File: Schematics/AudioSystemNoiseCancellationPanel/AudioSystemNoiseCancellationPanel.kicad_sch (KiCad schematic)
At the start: 7 parts, among them J1 AudioJack2, U1 OPA134

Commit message: progress check
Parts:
- removed J1: AudioJack2, symbol Connector_Audio:AudioJack2
- added C3: 1u, symbol Device:C_Small
- added C4: 0.1u, symbol Device:C_Small
- added U2: MIC5365-1.2YC5-TR, MIC5365-1.2YC5-TR:SOT65P210X110-5N, symbol AudioSystemSymbolLibrary:MIC5365-1.2YC5-TR
- C1: value 0.1u -> 1u
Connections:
- net GND: now also C3.2, C4.2, U2.2 (GND)
- net ANCSignal: now reaches R2.2, U1.6
- net -5VMic: now reaches U1.4 (V-)
- net +5VMic: now reaches U1.7 (V+)
- net +5VMic: now also C3.1, U2.1 (VIN), U2.3 (EN)
- net +1V1: no longer names the net of C1.1, MK1.3 (VDD)
- net +1V1: now also C4.1, U2.5 (VOUT)
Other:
- moved on the sheet: C2, MK1, R1, R2, U1

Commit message: power supply schematic possibly done
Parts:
- U2: footprint MIC5365-1.2YC5-TR:SOT65P210X110-5N -> AudioSystemFootprintLibrary:MIC5365-1.2YC5-TR
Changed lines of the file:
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@@
 		(on_board yes)
 		(dnp no)
-		(fields_autoplaced yes)
 		(property "Reference" "MK1"
 			(at 132.08 109.22 0)
@@
 			)
 		)
-		(property "Footprint" "MIC5365-1.2YC5-TR:SOT65P210X110-5N"
+		(property "Footprint" "AudioSystemFootprintLibrary:MIC5365-1.2YC5-TR"
 			(at 109.22 88.9 0)
 			(effects

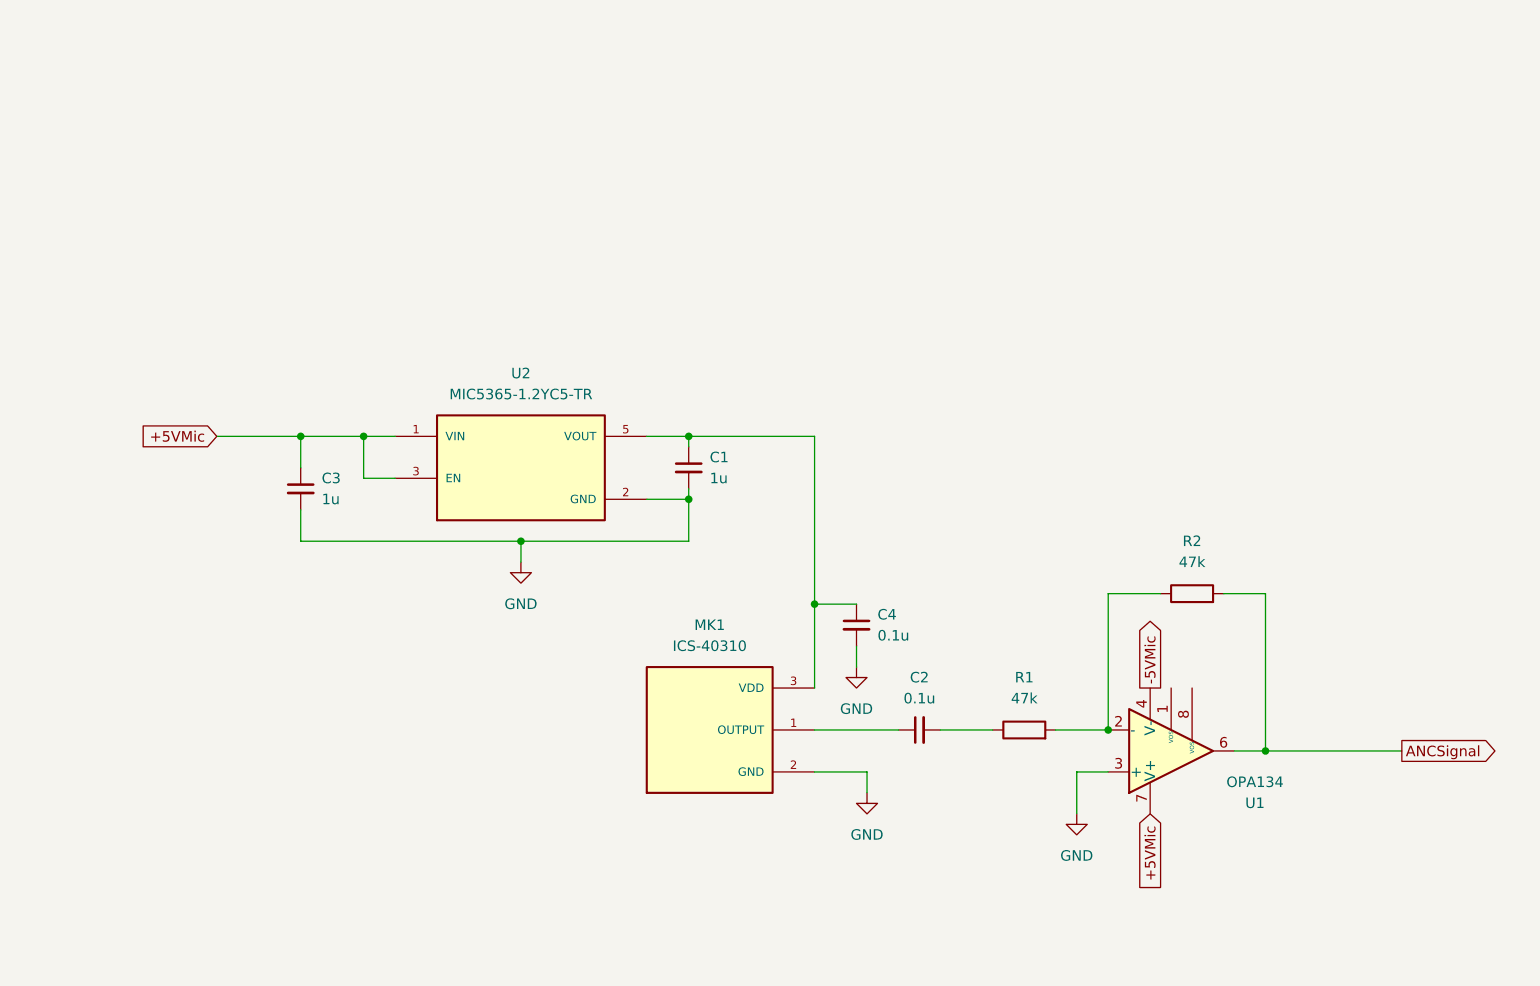
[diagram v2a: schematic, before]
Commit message: complete head unit schematic
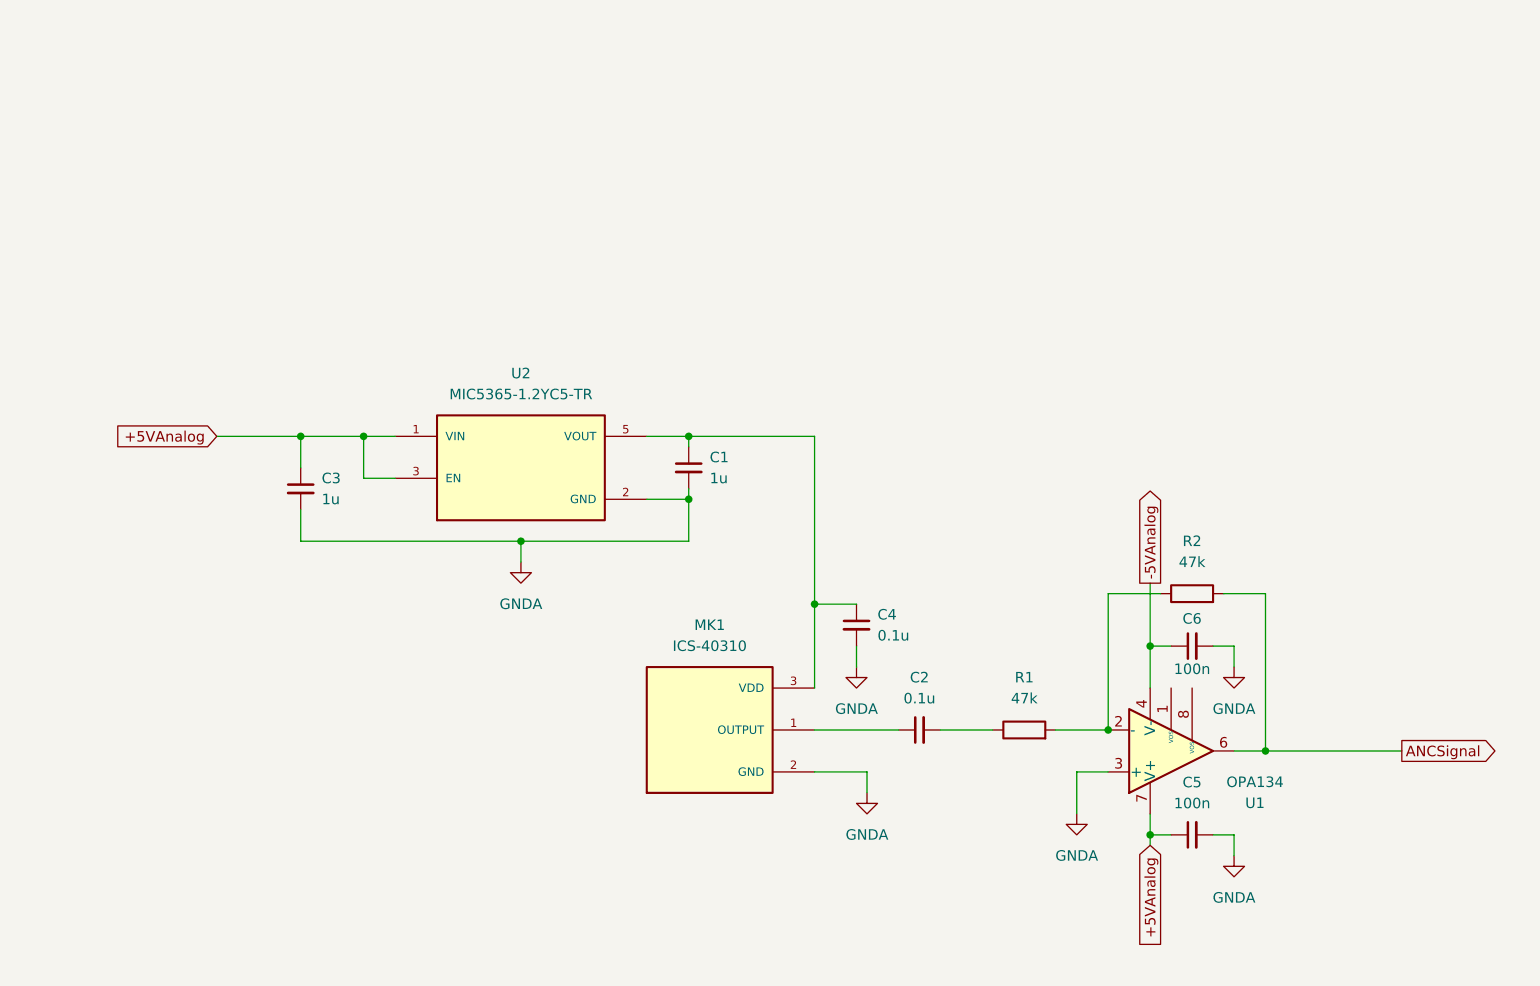
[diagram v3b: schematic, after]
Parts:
- added C5, C6: 100n, symbol Device:C_Small
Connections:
- net +5VMic renamed +5VAnalog
- net +5VAnalog: now also C5.1
- net -5VMic renamed -5VAnalog
- net -5VAnalog: now also C6.1
- net GND renamed GNDA
- net GNDA: now also C5.2, C6.2

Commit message: pcbs done
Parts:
- added J1: Conn_01x04_Pin, AudioSystemFootprintLibrary:4_Pad_Connector, symbol Connector:Conn_01x04_Pin
- C1, C2, C3, C4, C5, C6: footprint (none) -> Capacitor_SMD:C_0805_2012Metric_Pad1.18x1.45mm_HandSolder
- R1: footprint (none) -> Resistor_SMD:R_0805_2012Metric_Pad1.20x1.40mm_HandSolder
- R2: value 47k -> 820k; footprint (none) -> Resistor_SMD:R_0805_2012Metric_Pad1.20x1.40mm_HandSolder
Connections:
- net +5VAnalog: now also J1.1 (Pin_1)
- net -5VAnalog: now also J1.3 (Pin_3)
- net ANCSignal: now also J1.4 (Pin_4)
- net GNDA: now also J1.2 (Pin_2)
- no-connect marks 0 -> 2
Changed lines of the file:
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@@
 		(color 0 0 0 0)
 	)
+	(no_connect
+		(at 187.96 116.84)
+	)
+	(no_connect
+		(at 190.5 116.84)
+	)
+	(wire
+		(pts
+			(xy 158.75 74.93) (xy 175.26 74.93)
+		)
+		(stroke
+			(width 0)
+			(type default)
+		)
+	)
 	(wire
 		(pts
@@
 	(wire
 		(pts
-			(xy 151.13 127) (xy 151.13 129.54)
+			(xy 144.78 127) (xy 144.78 129.54)
 		)
 		(stroke
@@
 	(wire
 		(pts
-			(xy 144.78 127) (xy 151.13 127)
-		)
-		(stroke
-			(width 0)
-			(type default)
-		)
-	)
-	(wire
-		(pts
 			(xy 82.55 99.06) (xy 82.55 95.25)
 		)
@@
 			(width 0)
 			(type default)
+		)
+	)
+	(global_label "+5VAnalog"
+		(shape output)
+		(at 158.75 72.39 0)
+		(fields_autoplaced yes)
+		(effects
+			(font
+				(size 1.27 1.27)
+			)
+			(justify left)
+		)
+		(property "Intersheetrefs" "${INTERSHEET_REFS}"
+			(at 171.9555 72.39 0)
+			(effects
+				(font
+					(size 1.27 1.27)
+				)
+				(justify left)
+				(hide yes)
+			)
+		)
+	)
+	(global_label "ANCSignal"
+		(shape input)
+		(at 158.75 80.01 0)
+		(fields_autoplaced yes)
+		(effects
+			(font
+				(size 1.27 1.27)
+			)
+			(justify left)
+		)
+		(property "Intersheetrefs" "${INTERSHEET_REFS}"
+			(at 171.3508 80.01 0)
+			(effects
+				(font
+					(size 1.27 1.27)
+				)
+				(justify left)
+				(hide yes)
+			)
 		)
 	)
@@
 		)
 	)
+	(global_label "-5VAnalog"
+		(shape output)
+		(at 158.75 77.47 0)
+		(fields_autoplaced yes)
+		(effects
+			(font
+				(size 1.27 1.27)
+			)
+			(justify left)
+		)
+		(property "Intersheetrefs" "${INTERSHEET_REFS}"
+			(at 171.9555 77.47 0)
+			(effects
+				(font
+					(size 1.27 1.27)
+				)
+				(justify left)
+				(hide yes)
+			)
+		)
+	)
 	(global_label "+5VAnalog"
 		(shape input)
@@
 	)
 	(global_label "-5VAnalog"
-		(shape output)
+		(shape input)
 		(at 185.42 104.14 90)
 		(fields_autoplaced yes)
@@
 	(symbol
 		(lib_id "power:GNDA")
-		(at 151.13 129.54 0)
+		(at 144.78 129.54 0)
 		(unit 1)
 		(exclude_from_sim no)
@@
 		(fields_autoplaced yes)
 		(property "Reference" "#PWR05"
-			(at 151.13 135.89 0)
+			(at 144.78 135.89 0)
 			(effects
 				(font
@@
 		)
 		(property "Value" "GNDA"
-			(at 151.13 134.62 0)
+			(at 144.78 134.62 0)
 			(effects
 				(font
@@
 		)
 		(property "Footprint" ""
-			(at 151.13 129.54 0)
+			(at 144.78 129.54 0)
 			(effects
 				(font
@@
 		)
 		(property "Datasheet" ""
-			(at 151.13 129.54 0)
+			(at 144.78 129.54 0)
 			(effects
 				(font
@@
 		)
 		(property "Description" "Power symbol creates a global label with name \"GNDA\" , analog ground"
-			(at 151.13 129.54 0)
+			(at 144.78 129.54 0)
 			(effects
 				(font
@@
 				(path "/861f3109-942e-421c-acb5-8f0f964c2004"
 					(reference "#PWR06")
+					(unit 1)
+				)
+			)
+		)
+	)
+	(symbol
+		(lib_id "Connector:Conn_01x04_Pin")
+		(at 153.67 74.93 0)
+		(unit 1)
+		(exclude_from_sim no)
+		(in_bom yes)
+		(on_board yes)
+		(dnp no)
+		(fields_autoplaced yes)
+		(property "Reference" "J1"
+			(at 154.305 67.31 0)
+			(effects
+				(font
+					(size 1.27 1.27)
+				)
+			)
+		)
+		(property "Value" "Conn_01x04_Pin"
+			(at 154.305 69.85 0)
+			(effects
+				(font
+					(size 1.27 1.27)
+				)
+			)
+		)
+		(property "Footprint" "AudioSystemFootprintLibrary:4_Pad_Connector"
+			(at 153.67 74.93 0)
+			(effects
+				(font
+					(size 1.27 1.27)
+				)
+				(hide yes)
+			)
+		)
+		(property "Datasheet" "~"
+			(at 153.67 74.93 0)
+			(effects
+				(font
+					(size 1.27 1.27)
+				)
+				(hide yes)
+			)
+		)
+		(property "Description" "Generic connector, single row, 01x04, script generated"
+			(at 153.67 74.93 0)
+			(effects
+				(font
+					(size 1.27 1.27)
+				)
+				(hide yes)
+			)
+		)
+		(pin "2"
+		)
+		(pin "4"
+		)
+		(pin "1"
+		)
+		(pin "3"
+		)
+		(instances
+			(project ""
+				(path "/861f3109-942e-421c-acb5-8f0f964c2004"
+					(reference "J1")
 					(unit 1)
 				)
@@
 			)
 		)
-		(property "Footprint" ""
+		(property "Footprint" "Capacitor_SMD:C_0805_2012Metric_Pad1.18x1.45mm_HandSolder"
 			(at 82.55 92.71 0)
 			(effects
@@
 			)
 		)
-		(property "Footprint" ""
+		(property "Footprint" "Capacitor_SMD:C_0805_2012Metric_Pad1.18x1.45mm_HandSolder"
 			(at 149.86 109.22 0)
 			(effects
@@
 			)
 		)
-		(property "Footprint" ""
+		(property "Footprint" "Capacitor_SMD:C_0805_2012Metric_Pad1.18x1.45mm_HandSolder"
 			(at 190.5 111.76 0)
 			(effects
@@
 	)
 	(symbol
+		(lib_id "power:GNDA")
+		(at 175.26 74.93 0)
+		(unit 1)
+		(exclude_from_sim no)
+		(in_bom yes)
+		(on_board yes)
+		(dnp no)
+		(fields_autoplaced yes)
+		(property "Reference" "#PWR07"
+			(at 175.26 81.28 0)
+			(effects
+				(font
+					(size 1.27 1.27)
+				)
+				(hide yes)
+			)
+		)
+		(property "Value" "GNDA"
+			(at 175.26 80.01 0)
+			(effects
+				(font
+					(size 1.27 1.27)
+				)
+			)
+		)
+		(property "Footprint" ""
+			(at 175.26 74.93 0)
+			(effects
+				(font
+					(size 1.27 1.27)
+				)
+				(hide yes)
+			)
+		)
+		(property "Datasheet" ""
+			(at 175.26 74.93 0)
+			(effects
+				(font
+					(size 1.27 1.27)
+				)
+				(hide yes)
+			)
+		)
+		(property "Description" "Power symbol creates a global label with name \"GNDA\" , analog ground"
+			(at 175.26 74.93 0)
+			(effects
+				(font
+					(size 1.27 1.27)
+				)
+				(hide yes)
+			)
+		)
+		(pin "1"
+		)
+		(instances
+			(project "AudioSystemNoiseCancellationPanel"
+				(path "/861f3109-942e-421c-acb5-8f0f964c2004"
+					(reference "#PWR07")
+					(unit 1)
+				)
+			)
+		)
+	)
+	(symbol
 		(lib_id "Device:R")
 		(at 170.18 121.92 90)
@@
 			)
 		)
-		(property "Footprint" ""
+		(property "Footprint" "Resistor_SMD:R_0805_2012Metric_Pad1.20x1.40mm_HandSolder"
 			(at 170.18 123.698 90)
 			(effects
@@
 			)
 		)
-		(property "Footprint" ""
+		(property "Footprint" "Capacitor_SMD:C_0805_2012Metric_Pad1.18x1.45mm_HandSolder"
 			(at 129.54 90.17 0)
 			(effects
@@
 			)
 		)
-		(property "Footprint" ""
+		(property "Footprint" "Capacitor_SMD:C_0805_2012Metric_Pad1.18x1.45mm_HandSolder"
 			(at 190.5 134.62 0)
 			(effects
@@
 			)
 		)
-		(property "Value" "47k"
+		(property "Value" "820k"
 			(at 190.5 101.6 90)
 			(effects
@@
 			)
 		)
-		(property "Footprint" ""
+		(property "Footprint" "Resistor_SMD:R_0805_2012Metric_Pad1.20x1.40mm_HandSolder"
 			(at 190.5 107.188 90)
 			(effects
@@
 			)
 		)
-		(property "Footprint" ""
+		(property "Footprint" "Capacitor_SMD:C_0805_2012Metric_Pad1.18x1.45mm_HandSolder"
 			(at 157.48 121.92 0)
 			(effects
